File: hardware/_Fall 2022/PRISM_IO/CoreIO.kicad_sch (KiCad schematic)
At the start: 23 parts

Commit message: IO board
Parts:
- removed R?: R, symbol Device:R
- added R? (x4): 10k, symbol Device:R
- R1: value 10k -> 750
- R? (x3): value R -> 10k
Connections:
- net CONT 1: now also R?.1, R?.1, R?.2
- net GND: now also R?.2, R?.2, R?.2
- net V_IGNITOR: now also R?.1
- net at Q?.1 (D), U?.P$1 (+): now also R?.1

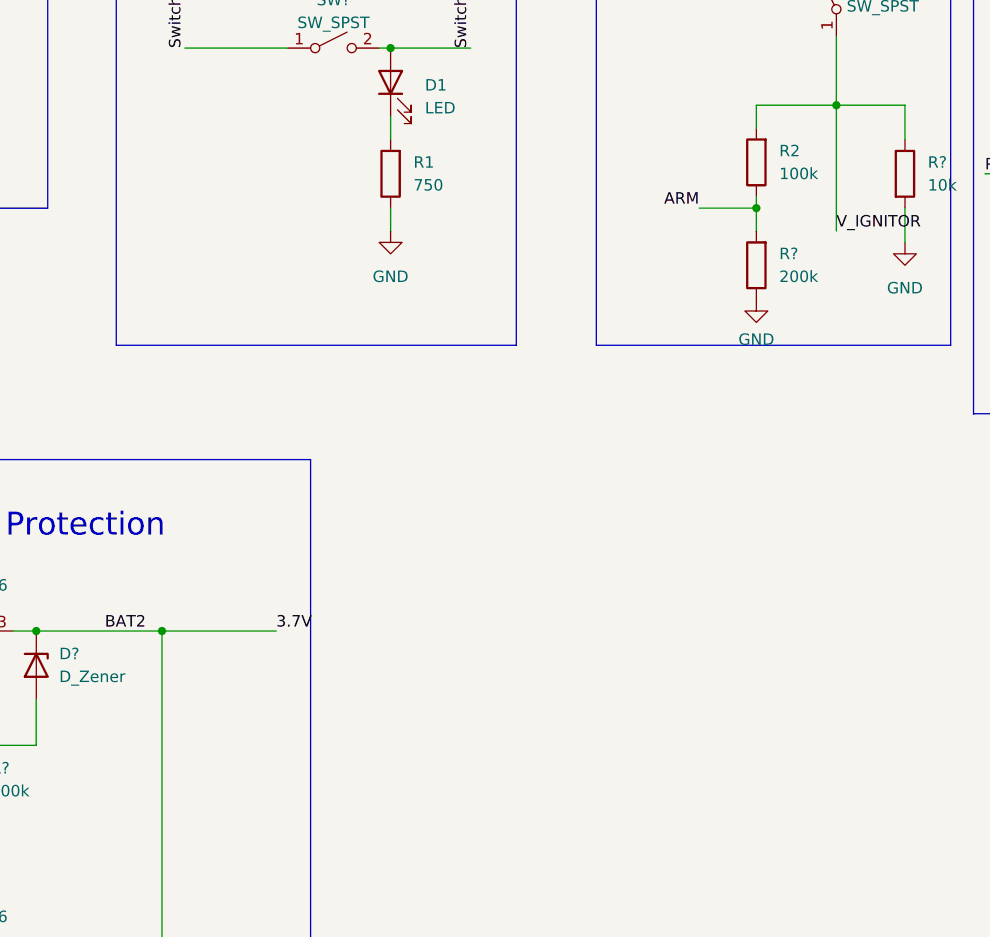
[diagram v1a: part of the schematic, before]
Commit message: changed resistor values on IO
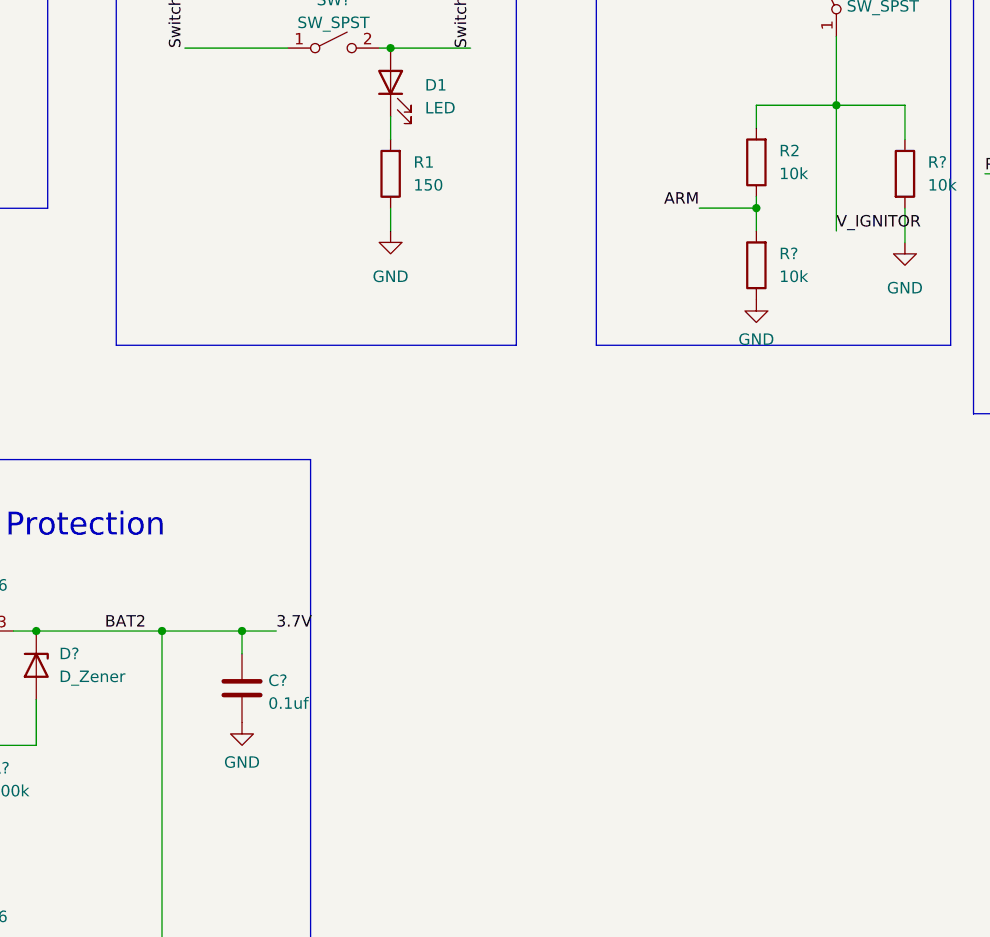
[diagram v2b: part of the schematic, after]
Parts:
- added C?: 0.1uf, symbol Device:C
- R1: value 750 -> 150
- R2: value 100k -> 10k
- R?: value 200k -> 10k
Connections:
- net 3.7V: now also C?.1
- net GND: now also C?.2
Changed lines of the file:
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@@
   (junction (at 52.07 129.54) (diameter 0) (color 0 0 0 0)
   )
+  (junction (at 82.55 116.84) (diameter 0) (color 0 0 0 0)
+  )
   (junction (at 204.47 63.5) (diameter 0) (color 0 0 0 0)
   )
@@
     (stroke (width 0) (type default) (color 0 0 0 0))
   )
-  (wire (pts (xy 73.66 116.84) (xy 86.36 116.84))
+  (wire (pts (xy 73.66 116.84) (xy 82.55 116.84))
     (stroke (width 0) (type default) (color 0 0 0 0))
   )
@@
     (stroke (width 0) (type default) (color 0 0 0 0))
   )
+  (wire (pts (xy 82.55 119.38) (xy 82.55 116.84))
+    (stroke (width 0) (type default) (color 0 0 0 0))
+  )
   (wire (pts (xy 24.13 116.84) (xy 24.13 153.67))
     (stroke (width 0) (type default) (color 0 0 0 0))
@@
   )
   (wire (pts (xy 139.7 60.96) (xy 139.7 58.42))
+    (stroke (width 0) (type default) (color 0 0 0 0))
+  )
+  (wire (pts (xy 82.55 116.84) (xy 86.36 116.84))
     (stroke (width 0) (type default) (color 0 0 0 0))
   )
@@
       (effects (font (size 1.27 1.27)) (justify right))
     )
-    (property "Value" "750" (id 1) (at 101.6 67.3099 0)
+    (property "Value" "150" (id 1) (at 101.6 67.3099 0)
       (effects (font (size 1.27 1.27)) (justify right))
     )
@@
     (pin "1")
   )
+  (symbol (lib_id "power:GND") (at 82.55 127 0) (unit 1)
+    (in_bom yes) (on_board yes) (fields_autoplaced)
+    (property "Reference" "#PWR?" (id 0) (at 82.55 133.35 0)
+      (effects (font (size 1.27 1.27)) hide)
+    )
+    (property "Value" "GND" (id 1) (at 82.55 131.4434 0))
+    (property "Footprint" "" (id 2) (at 82.55 127 0)
+      (effects (font (size 1.27 1.27)) hide)
+    )
+    (property "Datasheet" "" (id 3) (at 82.55 127 0)
+      (effects (font (size 1.27 1.27)) hide)
+    )
+    (pin "1")
+  )
   (symbol (lib_id "Device:Battery_Cell") (at 30.48 153.67 270) (unit 1)
     (in_bom yes) (on_board yes)
@@
     )
     (pin "1")
+  )
+  (symbol (lib_id "Device:C") (at 82.55 123.19 0) (unit 1)
+    (in_bom yes) (on_board yes) (fields_autoplaced)
+    (property "Reference" "C?" (id 0) (at 85.471 122.3553 0)
+      (effects (font (size 1.27 1.27)) (justify left))
+    )
+    (property "Value" "0.1uf" (id 1) (at 85.471 124.8922 0)
+      (effects (font (size 1.27 1.27)) (justify left))
+    )
+    (property "Footprint" "" (id 2) (at 83.5152 127 0)
+      (effects (font (size 1.27 1.27)) hide)
+    )
+    (property "Datasheet" "~" (id 3) (at 82.55 123.19 0)
+      (effects (font (size 1.27 1.27)) hide)
+    )
+    (pin "1")
+    (pin "2")
   )
   (symbol (lib_id "XT30:XT30UPB-M") (at 198.12 35.56 180) (unit 1)
@@
       (effects (font (size 1.27 1.27)) (justify right))
     )
-    (property "Value" "100k" (id 1) (at 142.24 66.0399 0)
+    (property "Value" "10k" (id 1) (at 142.24 66.0399 0)
       (effects (font (size 1.27 1.27)) (justify right))
     )
@@
       (effects (font (size 1.27 1.27)) (justify right))
     )
-    (property "Value" "200k" (id 1) (at 142.24 77.4699 0)
+    (property "Value" "10k" (id 1) (at 142.24 77.4699 0)
       (effects (font (size 1.27 1.27)) (justify right))
     )
@@
       (reference "#PWR?") (unit 1) (value "GND") (footprint "")
     )
+    (path "/737abce1-0f2a-40ce-a0da-56f898138790"
+      (reference "#PWR?") (unit 1) (value "GND") (footprint "")
+    )
     (path "/7fe982de-2526-4d6e-98c9-0d4536f646d3"
       (reference "#PWR?") (unit 1) (value "GND") (footprint "")
@@
       (reference "BT?") (unit 1) (value "~") (footprint "")
     )
+    (path "/848f4248-a48d-4a0d-b738-bbd118f52b82"
+      (reference "C?") (unit 1) (value "0.1uf") (footprint "")
+    )
     (path "/0b341755-06db-453d-817e-17956bf5f691"
       (reference "D1") (unit 1) (value "LED") (footprint "")
@@
     )
     (path "/2431e708-6d96-4879-b804-744396cc6ea4"
-      (reference "R1") (unit 1) (value "750") (footprint "")
+      (reference "R1") (unit 1) (value "150") (footprint "")
     )
     (path "/90e70778-87cc-48a2-850f-e02db16d561d"
-      (reference "R2") (unit 1) (value "100k") (footprint "")
+      (reference "R2") (unit 1) (value "10k") (footprint "")
     )
     (path "/209976c5-ce6d-4cb7-becd-ee216d196452"
@@
     )
     (path "/da01c7bf-6619-4764-9ff9-27e28e08c3c6"
-      (reference "R?") (unit 1) (value "200k") (footprint "")
+      (reference "R?") (unit 1) (value "10k") (footprint "")
     )
     (path "/ee9fdc92-5558-4243-8b3b-44df2d1be5ff"

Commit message: Reverse Current
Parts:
- removed BT?: ~, symbol Device:Battery_Cell
- removed C?: 0.1uf, symbol Device:C
- removed D? (x2): D_Zener, symbol Device:D_Zener
- removed Q? (x2): FQP27P06, Package_TO_SOT_THT:TO-220-3_Vertical, symbol Transistor_FET:FQP27P06
- removed R? (x2): 100k, symbol Device:R
- removed R?: 10k, symbol Device:R
- added BT2: ~, symbol Device:Battery_Cell
- added D2, D3: D_Schottky, symbol Device:D_Schottky
- added R3: R_15k, Resistor_SMD:R_0805_2012Metric_Pad1.20x1.40mm_HandSolder, symbol Device:R
- added R4: R_4.7k, Resistor_SMD:R_0805_2012Metric_Pad1.20x1.40mm_HandSolder, symbol Device:R
- J1: renamed from J?; value Conn_01x07_Female -> Conn_01x08_Female
- gave numbers to parts that had none: 14
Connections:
- net 3.7V: now also D1.2 (A)
- net CONT 1: no longer R10.2, R11.1
- net CONT 2: now also R10.2, R11.1
- net GND: now also R4.2; no longer D1.2 (A), R1.1
- net Switch1: now also R1.1, BT2.2 (-)
- net at BT1.1 (+): now also D2.2 (A)
- new net: BT2.1 (+), D3.2 (A)
- new net TPS2113A for Teensy power/IN1: D3.1 (K), R3.1
- new net TPS2113A for Teensy power/IN2: D2.1 (K)
- new net TPS2113A for Teensy power/VSNS: R3.2, R4.1
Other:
- added sheet TPS2113A for Teensy power (TPS2113A_Teesny.kicad_sch)
- note added: "Power Multiplexer"
- moved on the sheet: BT1, D1, R1, SW1
